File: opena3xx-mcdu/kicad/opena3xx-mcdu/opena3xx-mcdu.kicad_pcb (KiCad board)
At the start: 2 copper layers, 148 x 225 mm, 149 parts, among them J1 Conn_02x01, J2 Conn_02x01, J3 Conn_02x01, J4 Conn_02x01, J5 Conn_02x01, J6 Conn_02x01, J7 Conn_02x01, J8 Conn_02x01, J9 Conn_02x01, SW1 TLL-6A, SW10 TLL-6A, SW100 SW_MEC_5E, SW11 TLL-6A, SW12 TLL-6A, SW13 TLL-6A, SW14 TLL-6A, SW15 TLL-6A, SW16 TLL-6A, SW17 TLL-6A, SW18 TLL-6A, SW19 TLL-6A, SW2 TLL-6A, SW20 TLL-6A, SW21 TLL-6A, SW22 TLL-6A, SW23 TLL-6A, SW24 TLL-6A, SW25 TLL-6A, SW26 TLL-6A, SW27 TLL-6A, SW28 TLL-6A, SW29 TLL-6A, SW3 TLL-6A, SW30 TLL-6A, SW31 TLL-6A, SW32 TLL-6A, SW33 TLL-6A, SW34 TLL-6A, SW35 TLL-6A, SW36 TLL-6A, SW37 TLL-6A, SW38 TLL-6A, SW39 TLL-6A, SW4 TLL-6A, SW40 TLL-6A, SW41 TLL-6A, SW42 TLL-6A, SW43 TLL-6A, SW44 TLL-6A, SW45 TLL-6A, SW46 TLL-6A, SW47 TLL-6A, SW48 TLL-6A, SW49 TLL-6A, SW5 TLL-6A, SW50 TLL-6A, SW51 TLL-6A, SW52 TLL-6A, SW53 TLL-6A, SW54 TLL-6A, SW55 TLL-6A, SW56 TLL-6A, SW57 TLL-6A, SW58 TLL-6A, SW59 TLL-6A, SW6 TLL-6A, SW60 TLL-6A, SW61 TLL-6A, SW62 TLL-6A, SW63 TLL-6A, SW64 TLL-6A, SW65 TLL-6A, SW66 TLL-6A, SW67 TLL-6A, SW68 TLL-6A, SW69 TLL-6A, SW7 TLL-6A, SW70 TLL-6A, SW71 TLL-6A, SW72 TLL-6A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

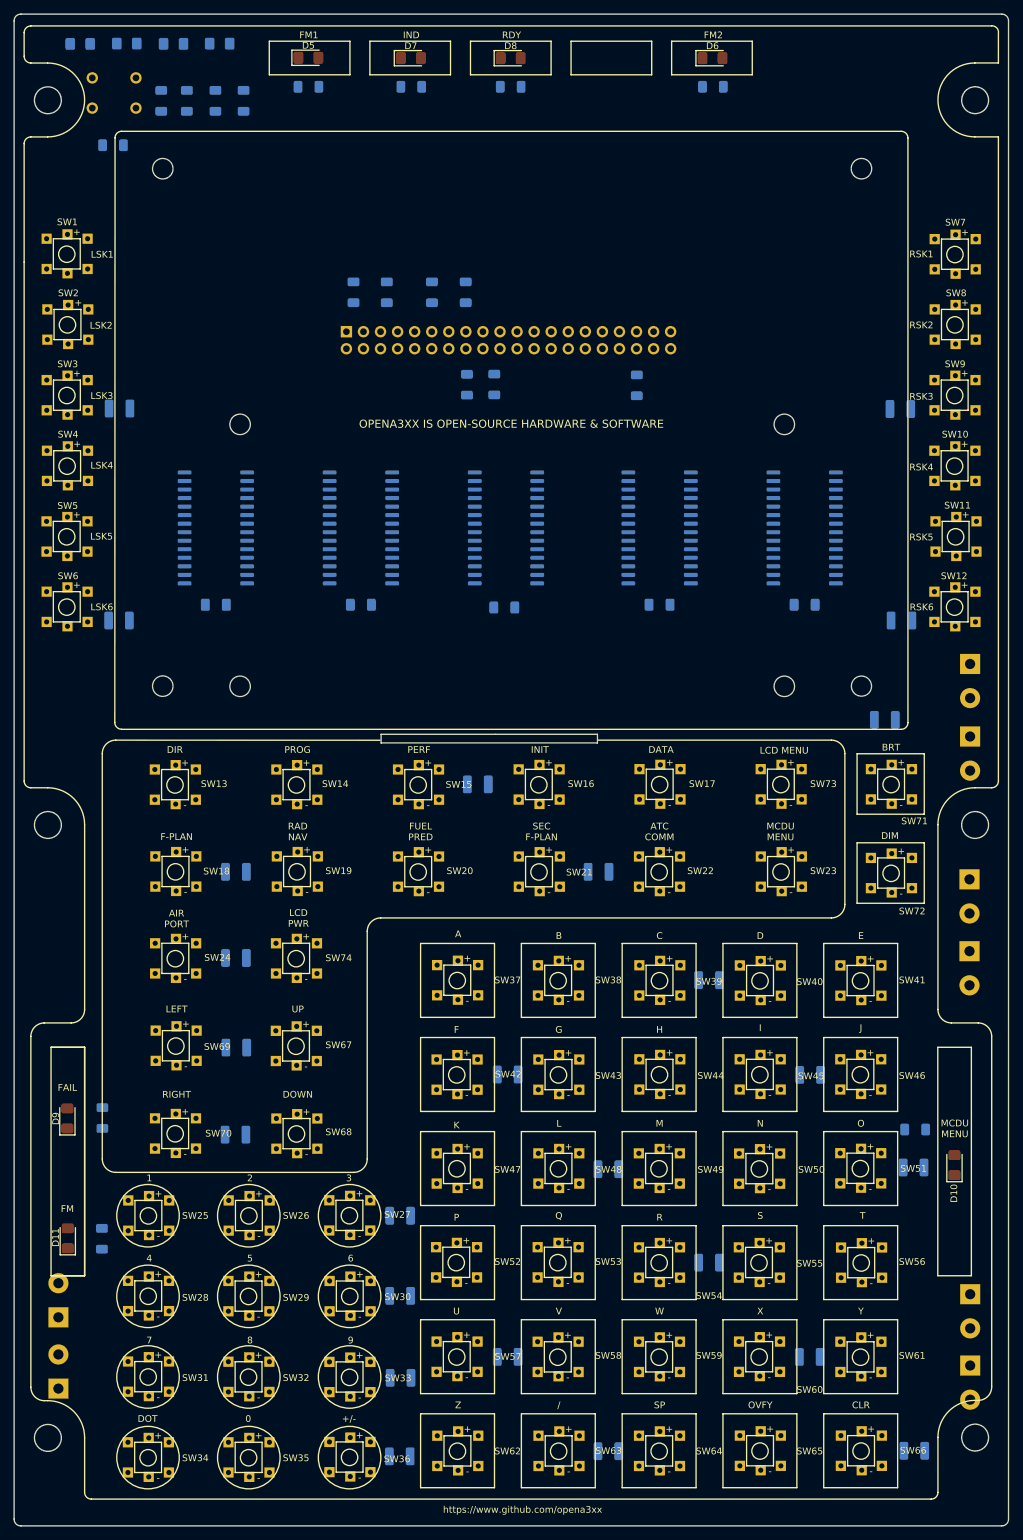
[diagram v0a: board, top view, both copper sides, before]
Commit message: Tacking OpenA3XX MCDU
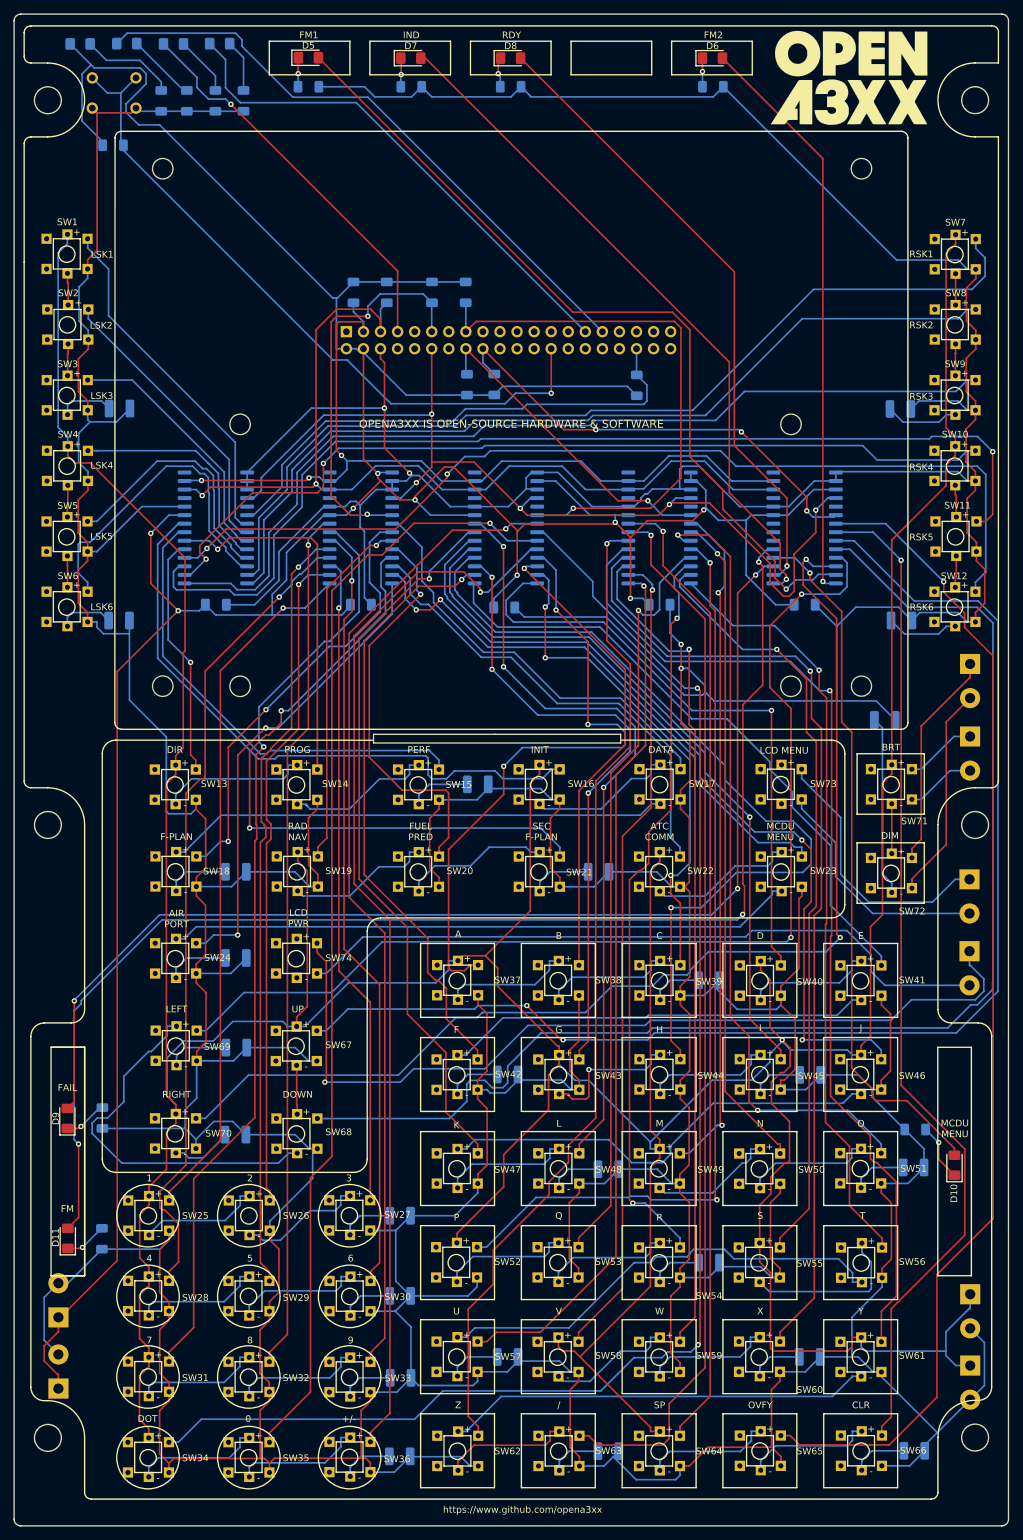
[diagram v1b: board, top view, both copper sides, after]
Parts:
- added G***: LOGO, opena3x:Logo, B.Cu at (156.5, 32.6)
- added G***: LOGO, opena3x:Logo, F.Cu at (155.0, 32.7)
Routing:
- net GND: track 0.00 -> 1685.7 mm, vias 0 -> 4
- net +12V: track 0.00 -> 775.6 mm, vias 0 -> 1
- net +5V: track 0.00 -> 534.0 mm, vias 0 -> 9
- net /BUS2-1: track 0.00 -> 217.5 mm, vias 0 -> 2
- net /BUS4-12: track 0.00 -> 196.5 mm, vias 0 -> 3
- net /BUS4-3: track 0.00 -> 194.8 mm
- net /BUS4-2: track 0.00 -> 192.2 mm, vias 0 -> 2
- net /BUS4-0: track 0.00 -> 174.2 mm, vias 0 -> 1
- net /BUS4-10: track 0.00 -> 173.1 mm, vias 0 -> 3
- net /BUS4-5: track 0.00 -> 170.8 mm, vias 0 -> 2
- net /BUS2-2: track 0.00 -> 166.4 mm, vias 0 -> 1
- net /BUS4-4: track 0.00 -> 161.3 mm, vias 0 -> 2
- net /BUS2-3: track 0.00 -> 158.8 mm, vias 0 -> 1
- net /BUS3-14: track 0.00 -> 157.9 mm, vias 0 -> 1
- net /BUS0-10: track 0.00 -> 156.1 mm, vias 0 -> 1
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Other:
- outline, holes or cut-outs redrawn

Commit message: Updating tracks and cleanup for MCDU
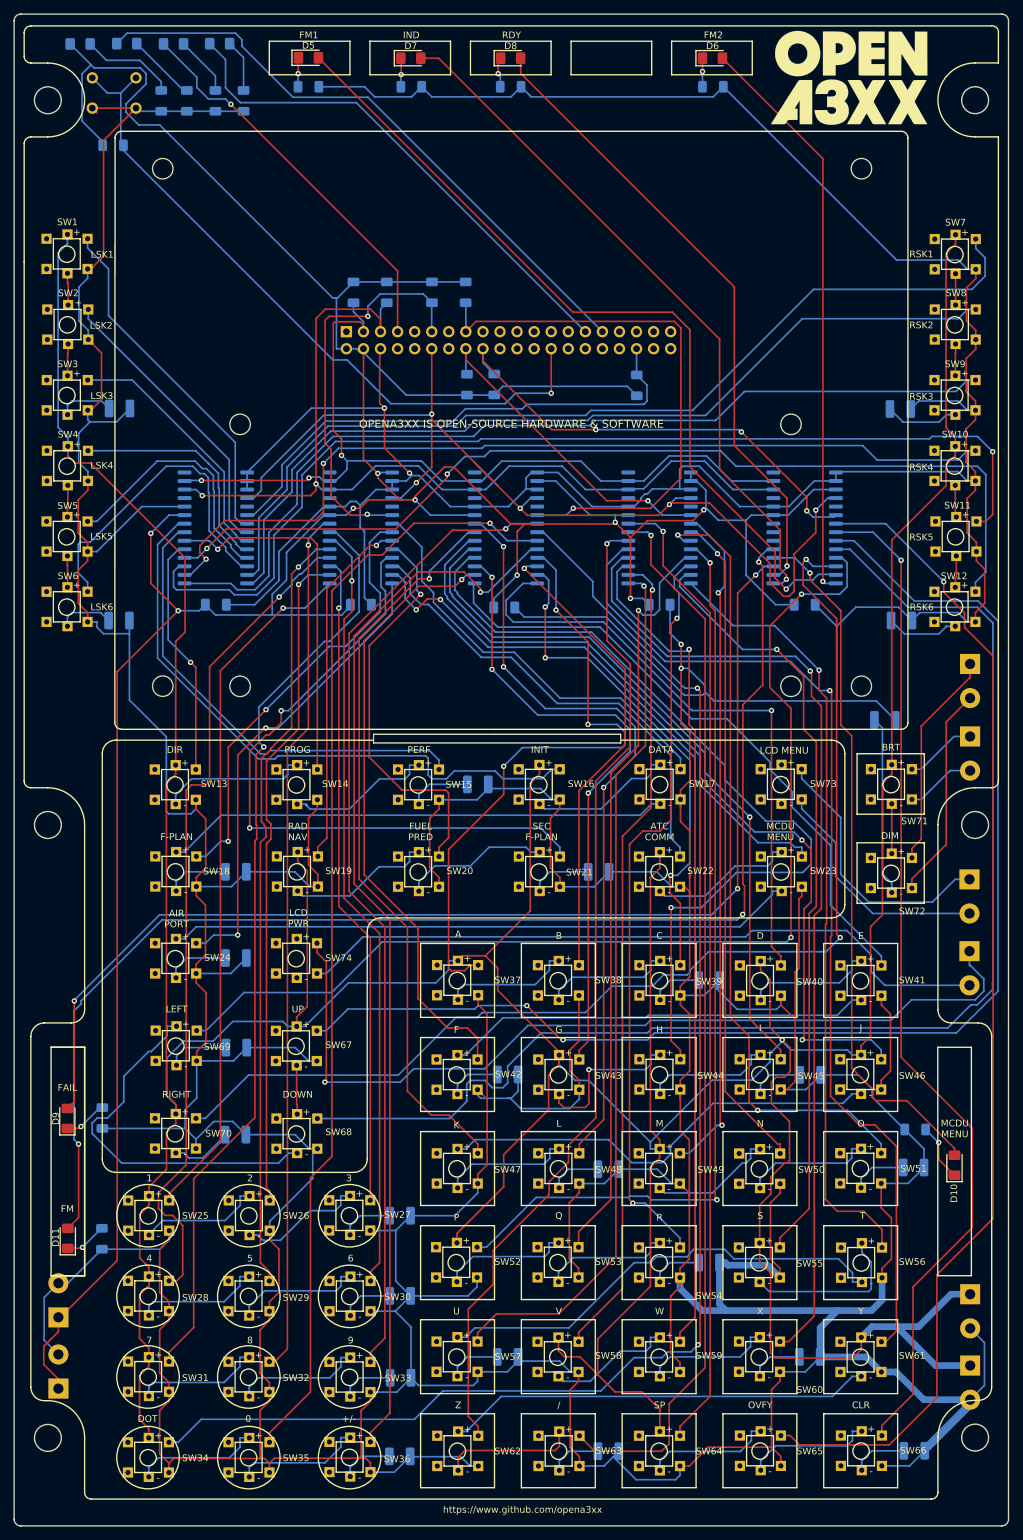
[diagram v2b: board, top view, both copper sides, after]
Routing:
- net GND: track 1685.7 -> 1759.5 mm
- net +12V: track 775.6 -> 787.7 mm
- net BUSES_RESET: track 148.8 -> 156.4 mm
- net +5V: track 534.0 -> 537.4 mm
- net /BUS1-11: track 121.5 -> 124.3 mm
- net Net-(SW43-Pad4): track 21.3 -> 23.7 mm
- net /BUS3-7: track 114.4 -> 116.7 mm
- net /BUS0-9: track 131.8 -> 134.0 mm
- net SCL: track 139.3 -> 140.9 mm
- net /BUS2-14: track 108.3 -> 109.9 mm
- net /BUS3-12: track 150.7 -> 152.3 mm
- net /BUS2-9: track 90.1 -> 91.6 mm
- net INT_BUS_1: track 58.8 -> 60.2 mm
- net /BUS3-5: track 110.6 -> 111.9 mm
- net /BUS3-14: track 157.9 -> 159.1 mm
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
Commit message: Cleanup MCDU PCB
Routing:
- net GND: track 1759.5 -> 1784.9 mm
- net Net-(SW68-Pad4): track 56.1 -> 60.3 mm
- net +5V: track 537.4 -> 541.1 mm
- net GENERAL_LED: track 91.9 -> 95.3 mm
- net Net-(R36-Pad1): track 9.27 -> 12.6 mm
- net /BUS2-8: track 94.1 -> 96.8 mm
- net /BUS0-15: track 93.0 -> 95.5 mm
- net Net-(R16-Pad1): track 10.9 -> 12.7 mm
- net /BUS0-6: track 140.8 -> 142.3 mm
- net Net-(SW26-Pad4): track 18.9 -> 20.4 mm
- net /BUS2-4: track 94.2 -> 95.6 mm
- net Net-(R15-Pad1): track 11.0 -> 12.3 mm
- net /BUS0-5: track 48.6 -> 49.8 mm
- net /BUS0-8: track 137.7 -> 138.8 mm
- net /BUS0-4: track 38.2 -> 39.1 mm
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
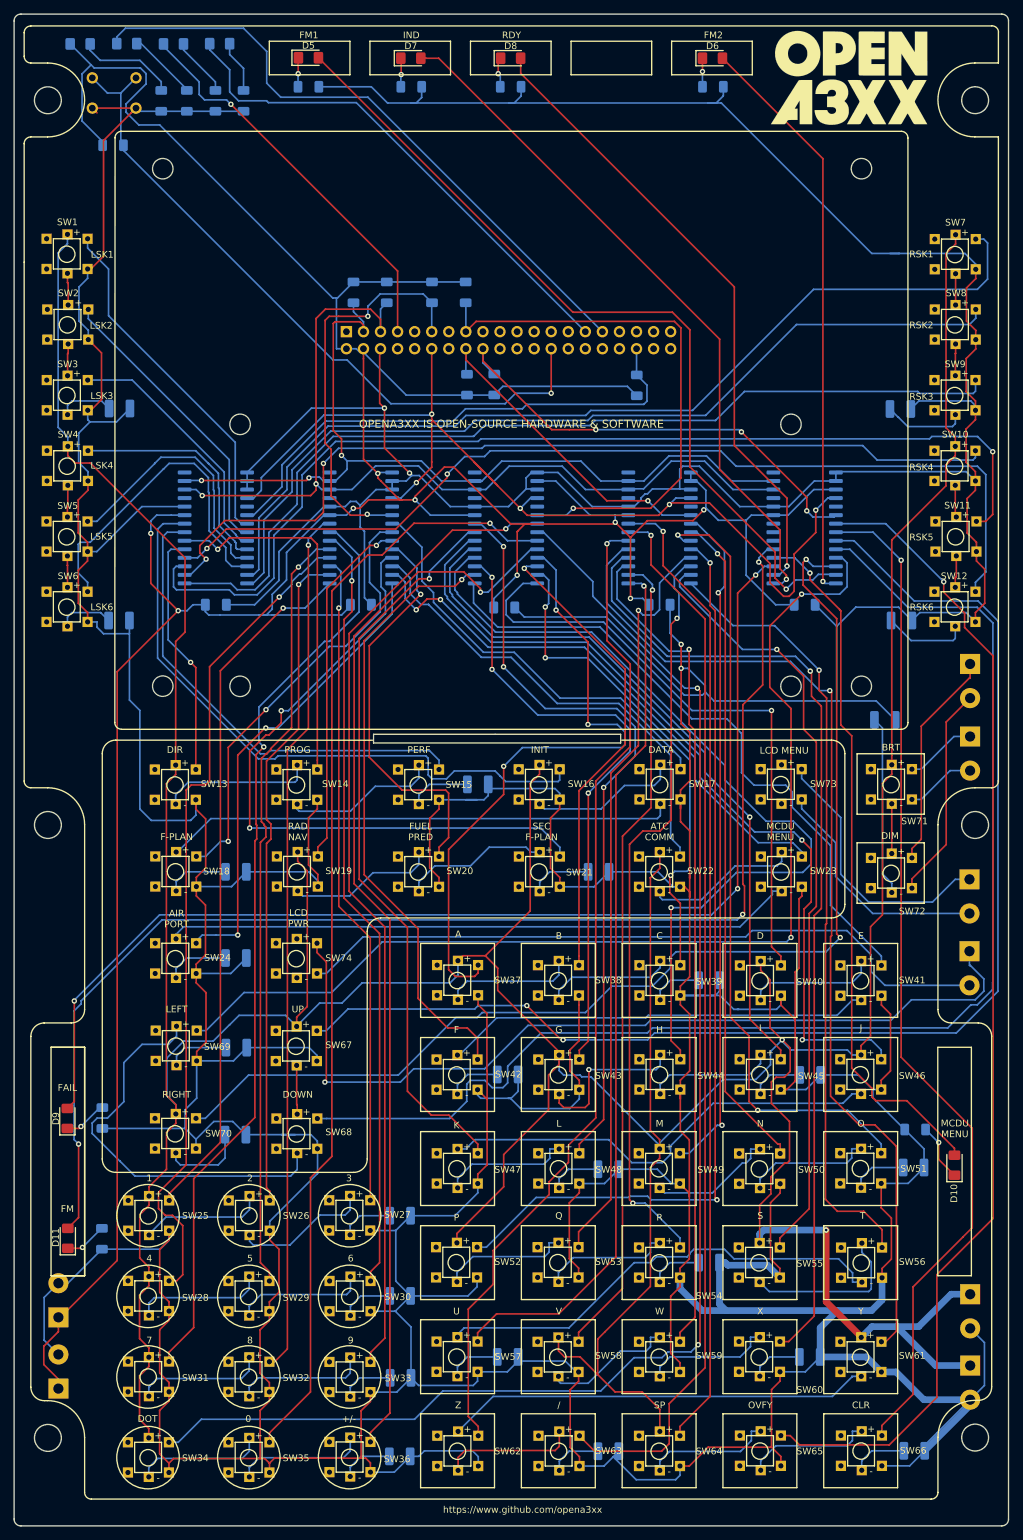
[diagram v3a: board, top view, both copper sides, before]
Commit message: WIP LED Backlight Widining
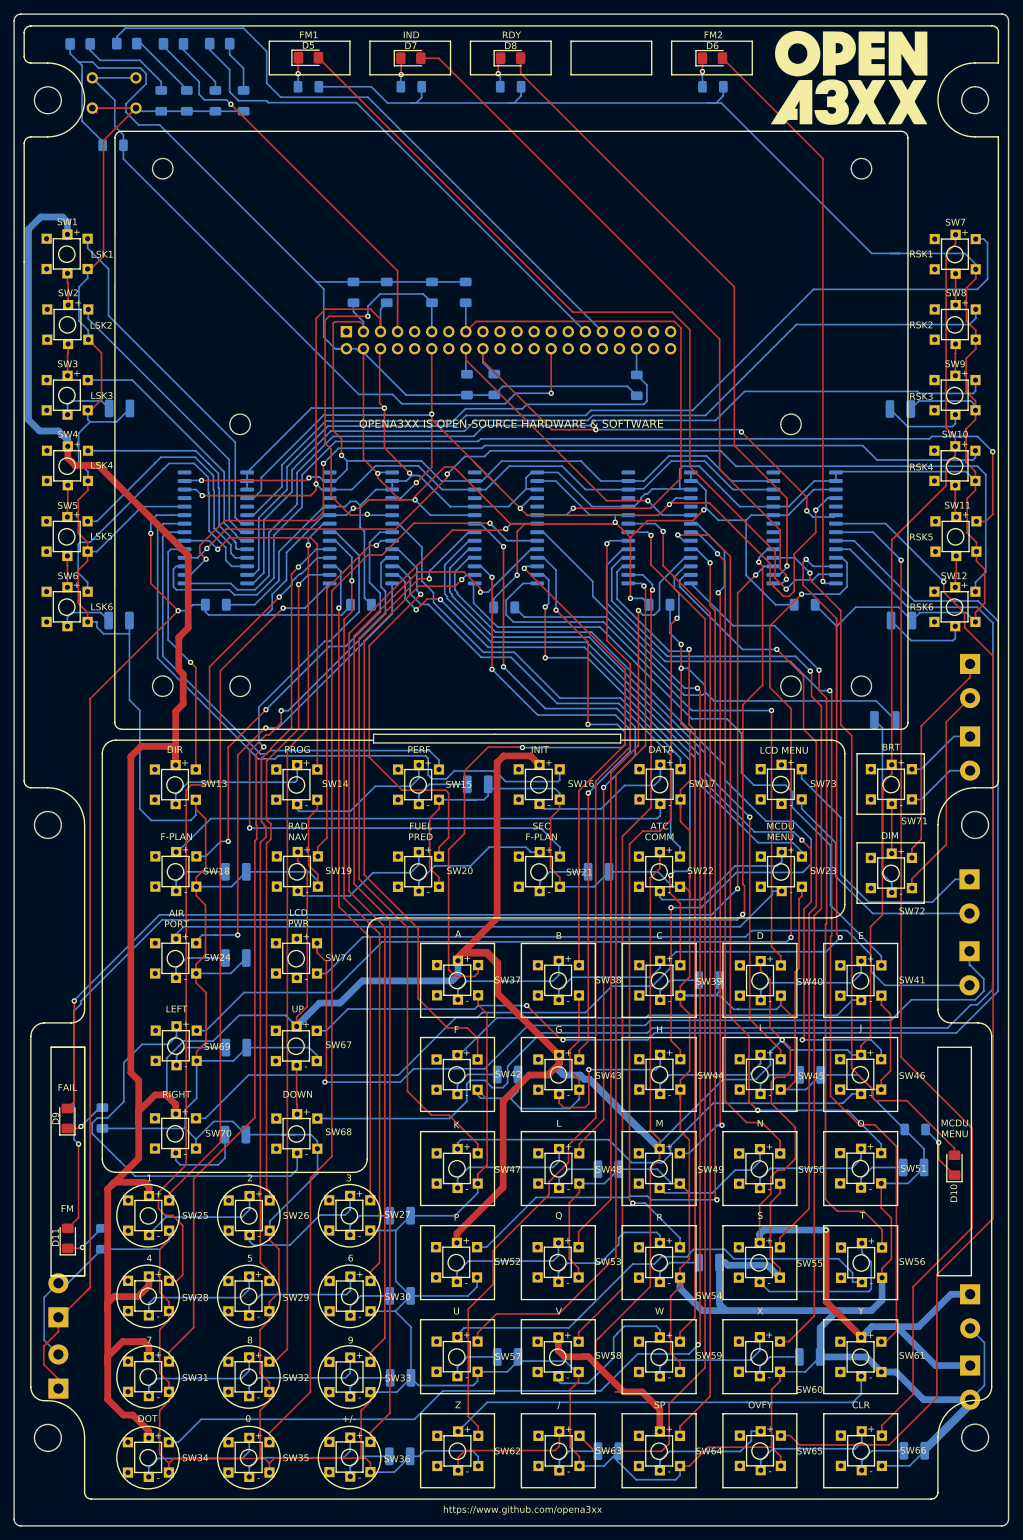
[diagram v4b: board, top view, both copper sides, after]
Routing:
- net +12V: track 787.0 -> 897.3 mm
- net RESET_SWITCH: track 103.6 -> 110.3 mm
- net +5V: track 541.1 -> 547.6 mm
- net /BUS2-4: track 95.6 -> 98.7 mm
- net Net-(SW58-Pad4): track 19.6 -> 22.6 mm
- net Net-(SW53-Pad4): track 19.1 -> 20.8 mm
- net Net-(SW61-Pad4): track 63.4 -> 64.9 mm
- net /BUS3-1: track 98.7 -> 99.8 mm
